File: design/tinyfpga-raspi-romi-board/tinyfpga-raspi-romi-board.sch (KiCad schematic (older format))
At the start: 72 parts, among them J1 TINYFPGA_J1, J10 ROMI_ENC_LEFT, J11 ROMI_ENC_RIGHT, J12 QTR_LEFT, J13 QTR_RIGHT, J14 SONAR_LEFT, J15 SONAR_RIGHT, J16 PWR_SEL1, J17 PWR_SEL0, J18 RPI_EXTRA, J19 ON_OFF, J2 TINYFPGA_J2, J20 ROMI_POWER, J3 Raspberry_Pi_2_3, J4 TINYFPGA_J4, J5 TINYFPGA_J5, J6 WP_JUMP, J7 ROMI_VSW, J8 FUSE_JUMP, J9 ROMI_MOTOR_DRIVE, Q1 2N7000, Q2 2N7000, Q3 2N7000, Q4 2N7000, Q5 2N7000, Q6 2N7000, Q7 2N7000, Q8 2N7000, SW2 SW_Push, SW3 SW_Push, SW4 SW_Push, U1 CAT24C128

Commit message: oh hey look its all through hole
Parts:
- removed J7: ROMI_VSW, Connector_PinHeader_2.54mm:PinHeader_2x03_P2.54mm_Vertical_SMD, symbol Connector_Generic:Conn_02x03_Odd_Even
- added J7: ROMI_VSW, Connector_PinHeader_2.54mm:PinHeader_2x08_P2.54mm_Vertical, symbol Connector_Generic:Conn_02x08_Odd_Even
- J20: footprint Connector_PinHeader_2.54mm:PinHeader_2x05_P2.54mm_Vertical_SMD -> Connector_PinHeader_2.54mm:PinHeader_2x05_P2.54mm_Vertical
- J4: footprint Connector_PinSocket_2.54mm:PinSocket_2x08_P2.54mm_Vertical_SMD -> Connector_PinSocket_2.54mm:PinSocket_2x08_P2.54mm_Vertical
- J5: footprint Connector_PinSocket_2.54mm:PinSocket_2x03_P2.54mm_Vertical_SMD -> Connector_PinSocket_2.54mm:PinSocket_2x03_P2.54mm_Vertical
- J9: footprint Connector_PinHeader_2.54mm:PinHeader_1x06_P2.54mm_Vertical_SMD_Pin1Left -> Connector_PinHeader_2.54mm:PinHeader_1x06_P2.54mm_Vertical
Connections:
- net +BATT: now also J7.1 (Pin_1), J7.3 (Pin_3), J7.5 (Pin_5)
- net FPGA_LED0: now also J2.14 (Pin_14); no longer J2.4 (Pin_4)
- net GND: now also J7.10 (Pin_10), J7.12 (Pin_12), J7.14 (Pin_14), J7.16 (Pin_16), J7.2 (Pin_2), J7.4 (Pin_4), J7.6 (Pin_6), J7.8 (Pin_8)
- net ROMI_3V3: now also J20.1 (Pin_1), J20.3 (Pin_3); no longer J20.7 (Pin_7), J20.9 (Pin_9)
- net ROMI_DIRL: now also J2.7 (Pin_7); no longer J2.6 (Pin_6)
- net ROMI_DIRR: now also J2.10 (Pin_10); no longer J2.9 (Pin_9)
- net ROMI_ENC_LA: now also J2.5 (Pin_5); no longer J2.11 (Pin_11)
- net ROMI_ENC_LB: now also J2.4 (Pin_4); no longer J2.12 (Pin_12)
- net ROMI_ENC_RB: now also J2.12 (Pin_12); no longer J2.14 (Pin_14)
- net ROMI_PWML: now also J2.8 (Pin_8); no longer J2.7 (Pin_7)
- net ROMI_PWMR: now also J2.11 (Pin_11); no longer J2.10 (Pin_10)
- net ROMI_~SLPL: now also J2.6 (Pin_6); no longer J2.5 (Pin_5)
- net ROMI_~SLPR: now also J2.9 (Pin_9); no longer J2.8 (Pin_8)
- net RPI_GPIO24: no longer J20.3 (Pin_3)
- net RPI_GPIO26: no longer J20.1 (Pin_1), J3.37 (GPIO26)
- net RPI_GPIO27: no longer J3.13 (GPIO27)
- new net: J7.11 (Pin_11), J7.7 (Pin_7), J7.9 (Pin_9)
- new net: J7.13 (Pin_13), J7.15 (Pin_15)
- new net ROMI_PG: J20.7 (Pin_7), J3.37 (GPIO26)
- new net ROMI_SHDN: J20.9 (Pin_9), J3.13 (GPIO27)
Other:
- moved on the sheet: A1, C1, C2, D1, D2, D3, D4, D5, D6, D7, D8, D9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

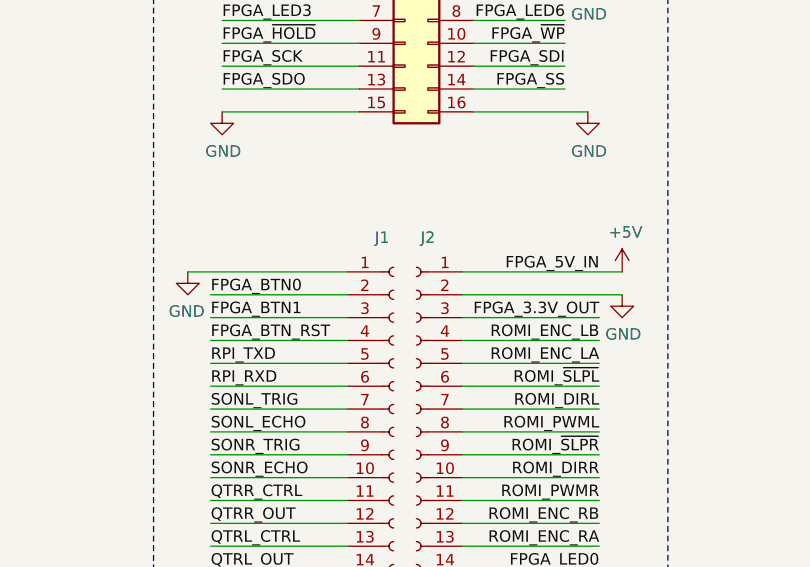
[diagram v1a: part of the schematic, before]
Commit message: updated mechanical dimensions, moved power and buttons
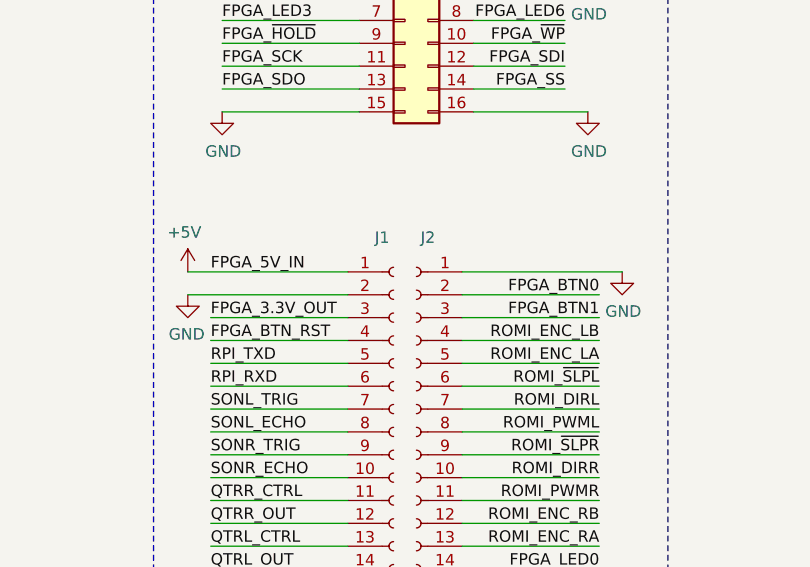
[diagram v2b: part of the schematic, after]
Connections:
- net +5V: now also J1.1 (Pin_1); no longer J2.1 (Pin_1)
- net FPGA_3.3V_OUT: now also J1.3 (Pin_3); no longer J2.3 (Pin_3)
- net FPGA_BTN0: now also J2.2 (Pin_2); no longer J1.2 (Pin_2)
- net FPGA_BTN1: now also J2.3 (Pin_3); no longer J1.3 (Pin_3)
- net GND: now also J1.2 (Pin_2), J2.1 (Pin_1); no longer J1.1 (Pin_1), J2.2 (Pin_2)
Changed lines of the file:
@@
 Wire Wire Line
 	9800 2850 9300 2850
-Text Label 10850 4900 2    50   ~ 0
-FPGA_5V_IN
-$Comp
-L power:GND #PWR03
-U 1 1 5CD97E36
-P 10950 5000
-F 0 "#PWR03" H 10950 4750 50  0001 C CNN
-F 1 "GND" H 10955 4827 50  0000 C CNN
-F 2 "" H 10950 5000 50  0001 C CNN
-F 3 "" H 10950 5000 50  0001 C CNN
-	1    10950 5000
-	1    0    0    -1
-$EndComp
-Wire Wire Line
-	10250 5000 10950 5000
-Wire Wire Line
-	10250 4900 10950 4900
-Wire Wire Line
-	10250 5100 10850 5100
 Text Label 9200 3600 0    50   ~ 0
 FPGA_3.3V_OUT
@@
 Wire Wire Line
 	1800 4900 1800 4950
-Text Label 10850 5100 2    50   ~ 0
-FPGA_3.3V_OUT
 $Comp
 L power:+5V #PWR021
@@
 Wire Wire Line
 	15250 6850 15800 6850
-$Comp
-L power:+5V #PWR01
-U 1 1 5CF4F72E
-P 10950 4900
-F 0 "#PWR01" H 10950 4750 50  0001 C CNN
-F 1 "+5V" H 10965 5073 50  0000 C CNN
-F 2 "" H 10950 4900 50  0001 C CNN
-F 3 "" H 10950 4900 50  0001 C CNN
-	1    10950 4900
-	1    0    0    -1
-$EndComp
 Text Label 14250 6550 2    50   ~ 0
 QTRL_CTRL
@@
 	-350 550  -350 3900
 Wire Wire Line
-	9150 5000 9750 5000
-Wire Wire Line
-	9150 5100 9750 5100
+	10850 5000 10250 5000
+Wire Wire Line
+	10850 5100 10250 5100
 Wire Wire Line
 	9150 5200 9750 5200
@@
 Text Label 9150 5200 0    50   ~ 0
 FPGA_BTN_RST
-Text Label 9150 5000 0    50   ~ 0
+Text Label 10850 5000 2    50   ~ 0
 FPGA_BTN0
-Text Label 9150 5100 0    50   ~ 0
+Text Label 10850 5100 2    50   ~ 0
 FPGA_BTN1
 $Comp
 L power:GND #PWR046
 U 1 1 5D01D33D
-P 9050 4900
-F 0 "#PWR046" H 9050 4650 50  0001 C CNN
-F 1 "GND" H 9055 4727 50  0000 C CNN
-F 2 "" H 9050 4900 50  0001 C CNN
-F 3 "" H 9050 4900 50  0001 C CNN
-	1    9050 4900
-	-1   0    0    -1
-$EndComp
-Wire Wire Line
-	9750 4900 9050 4900
+P 10950 4900
+F 0 "#PWR046" H 10950 4650 50  0001 C CNN
+F 1 "GND" H 10955 4727 50  0000 C CNN
+F 2 "" H 10950 4900 50  0001 C CNN
+F 3 "" H 10950 4900 50  0001 C CNN
+	1    10950 4900
+	1    0    0    -1
+$EndComp
+Wire Wire Line
+	10250 4900 10950 4900
 Text Notes 8900 2350 0    50   ~ 0
 TinyFPGA I/O Headers
@@
 Wire Notes Line
 	12850 -4150 8000 -4150
+Text Label 9150 4900 0    50   ~ 0
+FPGA_5V_IN
+$Comp
+L power:GND #PWR03
+U 1 1 5CD97E36
+P 9050 5000
+F 0 "#PWR03" H 9050 4750 50  0001 C CNN
+F 1 "GND" H 9055 4827 50  0000 C CNN
+F 2 "" H 9050 5000 50  0001 C CNN
+F 3 "" H 9050 5000 50  0001 C CNN
+	1    9050 5000
+	-1   0    0    -1
+$EndComp
+Wire Wire Line
+	9750 5000 9050 5000
+Wire Wire Line
+	9750 4900 9050 4900
+Wire Wire Line
+	9750 5100 9150 5100
+Text Label 9150 5100 0    50   ~ 0
+FPGA_3.3V_OUT
+$Comp
+L power:+5V #PWR01
+U 1 1 5CF4F72E
+P 9050 4900
+F 0 "#PWR01" H 9050 4750 50  0001 C CNN
+F 1 "+5V" H 9065 5073 50  0000 C CNN
+F 2 "" H 9050 4900 50  0001 C CNN
+F 3 "" H 9050 4900 50  0001 C CNN
+	1    9050 4900
+	-1   0    0    -1
+$EndComp
 $EndSCHEMATC
